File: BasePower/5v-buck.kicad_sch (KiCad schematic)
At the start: 14 parts, among them U2 TLVM13640

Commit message: BasePower design and inventory done
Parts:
- renumbered C17 to C19, C18 to C20, C19 to C21, C20 to C22, C21 to C23, C22 to C24, C23 to C25, C24 to C26, R11 to R15, R12 to R16, R13 to R17, R14 to R18, R15 to R19
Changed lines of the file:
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@@
 		(dnp no)
 		(fields_autoplaced yes)
-		(property "Reference" "C22"
+		(property "Reference" "C24"
 			(at 62.23 92.7162 0)
 			(effects
@@
 			(project "BasePower"
 				(path "/7a4c470e-f21a-4fdb-85db-575cfe7b758f/0d9f5d6e-bb0f-47ce-aa0a-0895cec808ef"
-					(reference "C22")
+					(reference "C24")
 					(unit 1)
 				)
@@
 		(dnp no)
 		(fields_autoplaced yes)
-		(property "Reference" "C21"
+		(property "Reference" "C23"
 			(at 45.72 92.7162 0)
 			(effects
@@
 			(project "BasePower"
 				(path "/7a4c470e-f21a-4fdb-85db-575cfe7b758f/0d9f5d6e-bb0f-47ce-aa0a-0895cec808ef"
-					(reference "C21")
+					(reference "C23")
 					(unit 1)
 				)
@@
 		(dnp no)
 		(fields_autoplaced yes)
-		(property "Reference" "C17"
+		(property "Reference" "C19"
 			(at 176.53 90.1762 0)
 			(effects
@@
 			(project "BasePower"
 				(path "/7a4c470e-f21a-4fdb-85db-575cfe7b758f/0d9f5d6e-bb0f-47ce-aa0a-0895cec808ef"
-					(reference "C17")
+					(reference "C19")
 					(unit 1)
 				)
@@
 		(on_board yes)
 		(dnp no)
-		(property "Reference" "R14"
+		(property "Reference" "R18"
 			(at 163.83 105.4099 0)
 			(effects
@@
 			(project "BasePower"
 				(path "/7a4c470e-f21a-4fdb-85db-575cfe7b758f/0d9f5d6e-bb0f-47ce-aa0a-0895cec808ef"
-					(reference "R14")
+					(reference "R18")
 					(unit 1)
 				)
@@
 		(on_board yes)
 		(dnp no)
-		(property "Reference" "C18"
+		(property "Reference" "C20"
 			(at 193.04 90.1762 0)
 			(effects
@@
 			(project "BasePower"
 				(path "/7a4c470e-f21a-4fdb-85db-575cfe7b758f/0d9f5d6e-bb0f-47ce-aa0a-0895cec808ef"
-					(reference "C18")
+					(reference "C20")
 					(unit 1)
 				)
@@
 		(dnp no)
 		(fields_autoplaced yes)
-		(property "Reference" "R15"
+		(property "Reference" "R19"
 			(at 100.33 109.2199 0)
 			(effects
@@
 			(project "BasePower"
 				(path "/7a4c470e-f21a-4fdb-85db-575cfe7b758f/0d9f5d6e-bb0f-47ce-aa0a-0895cec808ef"
-					(reference "R15")
+					(reference "R19")
 					(unit 1)
 				)
@@
 		(dnp no)
 		(fields_autoplaced yes)
-		(property "Reference" "R13"
+		(property "Reference" "R17"
 			(at 142.24 102.8699 0)
 			(effects
@@
 			(project "BasePower"
 				(path "/7a4c470e-f21a-4fdb-85db-575cfe7b758f/0d9f5d6e-bb0f-47ce-aa0a-0895cec808ef"
-					(reference "R13")
+					(reference "R17")
 					(unit 1)
 				)
@@
 		(dnp no)
 		(fields_autoplaced yes)
-		(property "Reference" "C24"
+		(property "Reference" "C26"
 			(at 151.13 105.4162 0)
 			(effects
@@
 			(project "BasePower"
 				(path "/7a4c470e-f21a-4fdb-85db-575cfe7b758f/0d9f5d6e-bb0f-47ce-aa0a-0895cec808ef"
-					(reference "C24")
+					(reference "C26")
 					(unit 1)
 				)
@@
 		(dnp no)
 		(fields_autoplaced yes)
-		(property "Reference" "C20"
+		(property "Reference" "C22"
 			(at 226.06 89.2809 0)
 			(effects
@@
 			(project "BasePower"
 				(path "/7a4c470e-f21a-4fdb-85db-575cfe7b758f/0d9f5d6e-bb0f-47ce-aa0a-0895cec808ef"
-					(reference "C20")
+					(reference "C22")
 					(unit 1)
 				)
@@
 		(dnp no)
 		(fields_autoplaced yes)
-		(property "Reference" "#PWR07"
+		(property "Reference" "#PWR012"
 			(at 120.65 127 0)
 			(effects
@@
 			(project "BasePower"
 				(path "/7a4c470e-f21a-4fdb-85db-575cfe7b758f/0d9f5d6e-bb0f-47ce-aa0a-0895cec808ef"
-					(reference "#PWR07")
+					(reference "#PWR012")
 					(unit 1)
 				)
@@
 		(dnp no)
 		(fields_autoplaced yes)
-		(property "Reference" "C23"
+		(property "Reference" "C25"
 			(at 87.63 104.1462 0)
 			(effects
@@
 			(project "BasePower"
 				(path "/7a4c470e-f21a-4fdb-85db-575cfe7b758f/0d9f5d6e-bb0f-47ce-aa0a-0895cec808ef"
-					(reference "C23")
+					(reference "C25")
 					(unit 1)
 				)
@@
 		(dnp no)
 		(fields_autoplaced yes)
-		(property "Reference" "R11"
+		(property "Reference" "R15"
 			(at 163.83 90.1699 0)
 			(effects
@@
 			(project "BasePower"
 				(path "/7a4c470e-f21a-4fdb-85db-575cfe7b758f/0d9f5d6e-bb0f-47ce-aa0a-0895cec808ef"
-					(reference "R11")
+					(reference "R15")
 					(unit 1)
 				)
@@
 		(on_board yes)
 		(dnp no)
-		(property "Reference" "C19"
+		(property "Reference" "C21"
 			(at 208.28 90.1762 0)
 			(effects
@@
 			(project "BasePower"
 				(path "/7a4c470e-f21a-4fdb-85db-575cfe7b758f/0d9f5d6e-bb0f-47ce-aa0a-0895cec808ef"
-					(reference "C19")
+					(reference "C21")
 					(unit 1)
 				)
@@
 		(on_board yes)
 		(dnp no)
-		(property "Reference" "R12"
+		(property "Reference" "R16"
 			(at 247.65 93.9799 0)
 			(effects
@@
 			(project "BasePower"
 				(path "/7a4c470e-f21a-4fdb-85db-575cfe7b758f/0d9f5d6e-bb0f-47ce-aa0a-0895cec808ef"
-					(reference "R12")
-					(unit 1)
-				)
+					(reference "R16")
+					(unit 1)
+				)

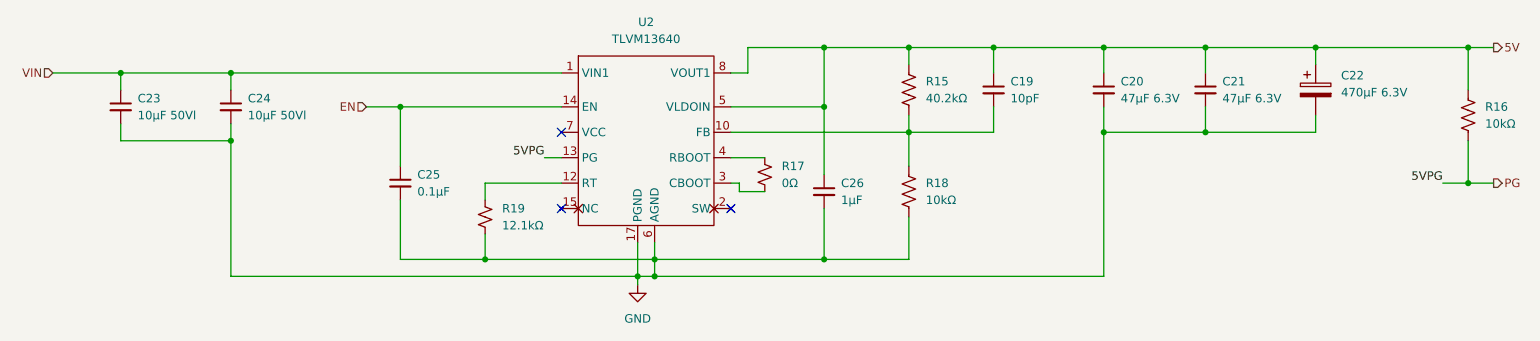
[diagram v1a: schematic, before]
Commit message: BasePower v1.2 + inventory
Added 12V clean LDO and improved power good display
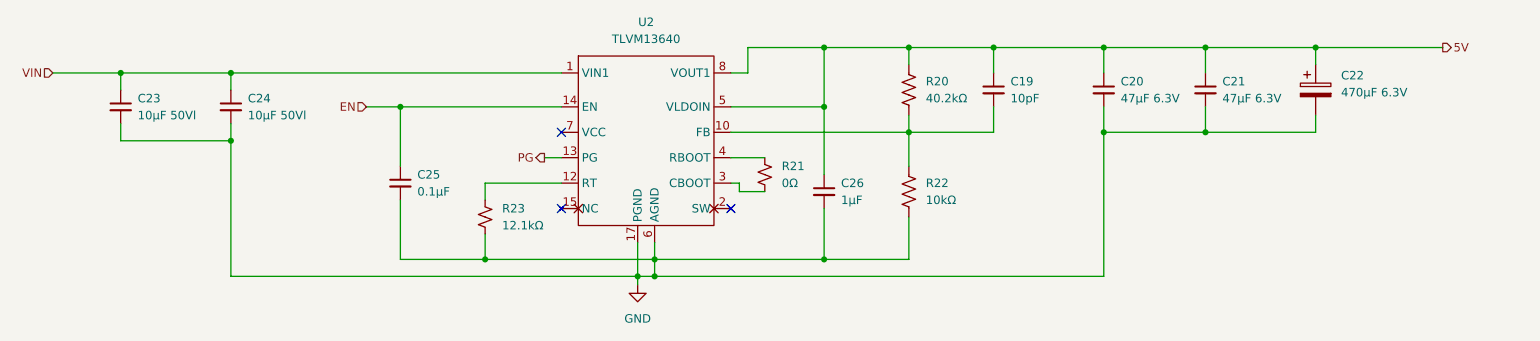
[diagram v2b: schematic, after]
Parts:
- removed R16: 10kΩ, Resistor_SMD:R_0603_1608Metric, symbol Device:R_US
- renumbered R15 to R20, R17 to R21, R18 to R22, R19 to R23
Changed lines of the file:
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@@
-	)
-	(junction
-		(at 245.11 85.09)
-		(diameter 0)
-		(color 0 0 0 0)
 	)
 	(junction
@@
 	)
 	(junction
-		(at 245.11 105.41)
-		(diameter 0)
-		(color 0 0 0 0)
-	)
-	(junction
 		(at 120.65 119.38)
 		(diameter 0)
@@
 	(wire
 		(pts
-			(xy 245.11 105.41) (xy 248.92 105.41)
-		)
-		(stroke
-			(width 0)
-			(type default)
-		)
-	)
-	(wire
-		(pts
 			(xy 148.59 116.84) (xy 161.29 116.84)
 		)
@@
 	(wire
 		(pts
-			(xy 245.11 85.09) (xy 245.11 91.44)
-		)
-		(stroke
-			(width 0)
-			(type default)
-		)
-	)
-	(wire
-		(pts
 			(xy 59.69 88.9) (xy 59.69 91.44)
 		)
@@
 	(wire
 		(pts
-			(xy 245.11 99.06) (xy 245.11 105.41)
-		)
-		(stroke
-			(width 0)
-			(type default)
-		)
-	)
-	(wire
-		(pts
 			(xy 109.22 105.41) (xy 97.79 105.41)
 		)
@@
 	(wire
 		(pts
-			(xy 248.92 85.09) (xy 245.11 85.09)
-		)
-		(stroke
-			(width 0)
-			(type default)
-		)
-	)
-	(wire
-		(pts
-			(xy 245.11 85.09) (xy 222.25 85.09)
-		)
-		(stroke
-			(width 0)
-			(type default)
-		)
-	)
-	(wire
-		(pts
-			(xy 241.3 105.41) (xy 245.11 105.41)
+			(xy 222.25 85.09) (xy 241.3 85.09)
 		)
 		(stroke
@@
 			(width 0)
 			(type default)
-		)
-	)
-	(label "5VPG"
-		(at 106.68 101.6 180)
-		(fields_autoplaced yes)
-		(effects
-			(font
-				(size 1.27 1.27)
-			)
-			(justify right bottom)
-		)
-	)
-	(label "5VPG"
-		(at 241.3 105.41 180)
-		(fields_autoplaced yes)
-		(effects
-			(font
-				(size 1.27 1.27)
-			)
-			(justify right bottom)
 		)
 	)
@@
 	(hierarchical_label "PG"
 		(shape output)
-		(at 248.92 105.41 0)
+		(at 106.68 101.6 180)
 		(fields_autoplaced yes)
 		(effects
@@
 				(size 1.27 1.27)
 			)
-			(justify left)
+			(justify right)
 		)
 	)
 	(hierarchical_label "5V"
 		(shape output)
-		(at 248.92 85.09 0)
+		(at 241.3 85.09 0)
 		(fields_autoplaced yes)
 		(effects
@@
 		(on_board yes)
 		(dnp no)
-		(property "Reference" "R18"
+		(property "Reference" "R22"
 			(at 163.83 105.4099 0)
 			(effects
@@
 			(project "BasePower"
 				(path "/7a4c470e-f21a-4fdb-85db-575cfe7b758f/0d9f5d6e-bb0f-47ce-aa0a-0895cec808ef"
-					(reference "R18")
+					(reference "R22")
 					(unit 1)
 				)
@@
 		(dnp no)
 		(fields_autoplaced yes)
-		(property "Reference" "R19"
+		(property "Reference" "R23"
 			(at 100.33 109.2199 0)
 			(effects
@@
 			(project "BasePower"
 				(path "/7a4c470e-f21a-4fdb-85db-575cfe7b758f/0d9f5d6e-bb0f-47ce-aa0a-0895cec808ef"
-					(reference "R19")
+					(reference "R23")
 					(unit 1)
 				)
@@
 		(dnp no)
 		(fields_autoplaced yes)
-		(property "Reference" "R17"
+		(property "Reference" "R21"
 			(at 142.24 102.8699 0)
 			(effects
@@
 			(project "BasePower"
 				(path "/7a4c470e-f21a-4fdb-85db-575cfe7b758f/0d9f5d6e-bb0f-47ce-aa0a-0895cec808ef"
-					(reference "R17")
+					(reference "R21")
 					(unit 1)
 				)
@@
 		(dnp no)
 		(fields_autoplaced yes)
-		(property "Reference" "#PWR012"
+		(property "Reference" "#PWR013"
 			(at 120.65 127 0)
 			(effects
@@
 			(project "BasePower"
 				(path "/7a4c470e-f21a-4fdb-85db-575cfe7b758f/0d9f5d6e-bb0f-47ce-aa0a-0895cec808ef"
-					(reference "#PWR012")
+					(reference "#PWR013")
 					(unit 1)
 				)
@@
 		(dnp no)
 		(fields_autoplaced yes)
-		(property "Reference" "R15"
+		(property "Reference" "R20"
 			(at 163.83 90.1699 0)
 			(effects
@@
 			(project "BasePower"
 				(path "/7a4c470e-f21a-4fdb-85db-575cfe7b758f/0d9f5d6e-bb0f-47ce-aa0a-0895cec808ef"
-					(reference "R15")
+					(reference "R20")
 					(unit 1)
 				)
@@
 					(unit 1)
 				)
-			)
-		)
-	)
-	(symbol
-		(lib_id "Device:R_US")
-		(at 245.11 95.25 0)
-		(unit 1)
-		(exclude_from_sim no)
-		(in_bom yes)
-		(on_board yes)
-		(dnp no)
-		(property "Reference" "R16"
-			(at 247.65 93.9799 0)
-			(effects
-				(font
-					(size 1.27 1.27)
-				)
-				(justify left)
-			)
-		)
-		(property "Value" "10kΩ"
-			(at 247.65 96.5199 0)
-			(effects
-				(font
-					(size 1.27 1.27)
-				)
-				(justify left)
-			)
-		)
-		(property "Footprint" "Resistor_SMD:R_0603_1608Metric"
-			(at 246.126 95.504 90)
-			(effects
-				(font
-					(size 1.27 1.27)
-				)
-				(hide yes)
-			)
-		)
-		(property "Datasheet" "~"
-			(at 245.11 95.25 0)
-			(effects
-				(font
-					(size 1.27 1.27)
-				)
-				(hide yes)
-			)
-		)
-		(property "Description" "Resistor, US symbol"
-			(at 245.11 95.25 0)
-			(effects
-				(font
-					(size 1.27 1.27)
-				)
-				(hide yes)
-			)
-		)
-		(pin "1"
-		)
-		(pin "2"
-		)
-		(instances
-			(project "BasePower"
-				(path "/7a4c470e-f21a-4fdb-85db-575cfe7b758f/0d9f5d6e-bb0f-47ce-aa0a-0895cec808ef"
-					(reference "R16")
-					(unit 1)
-				)
